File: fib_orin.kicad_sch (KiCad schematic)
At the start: 8 parts, among them J1201 Orin Nano

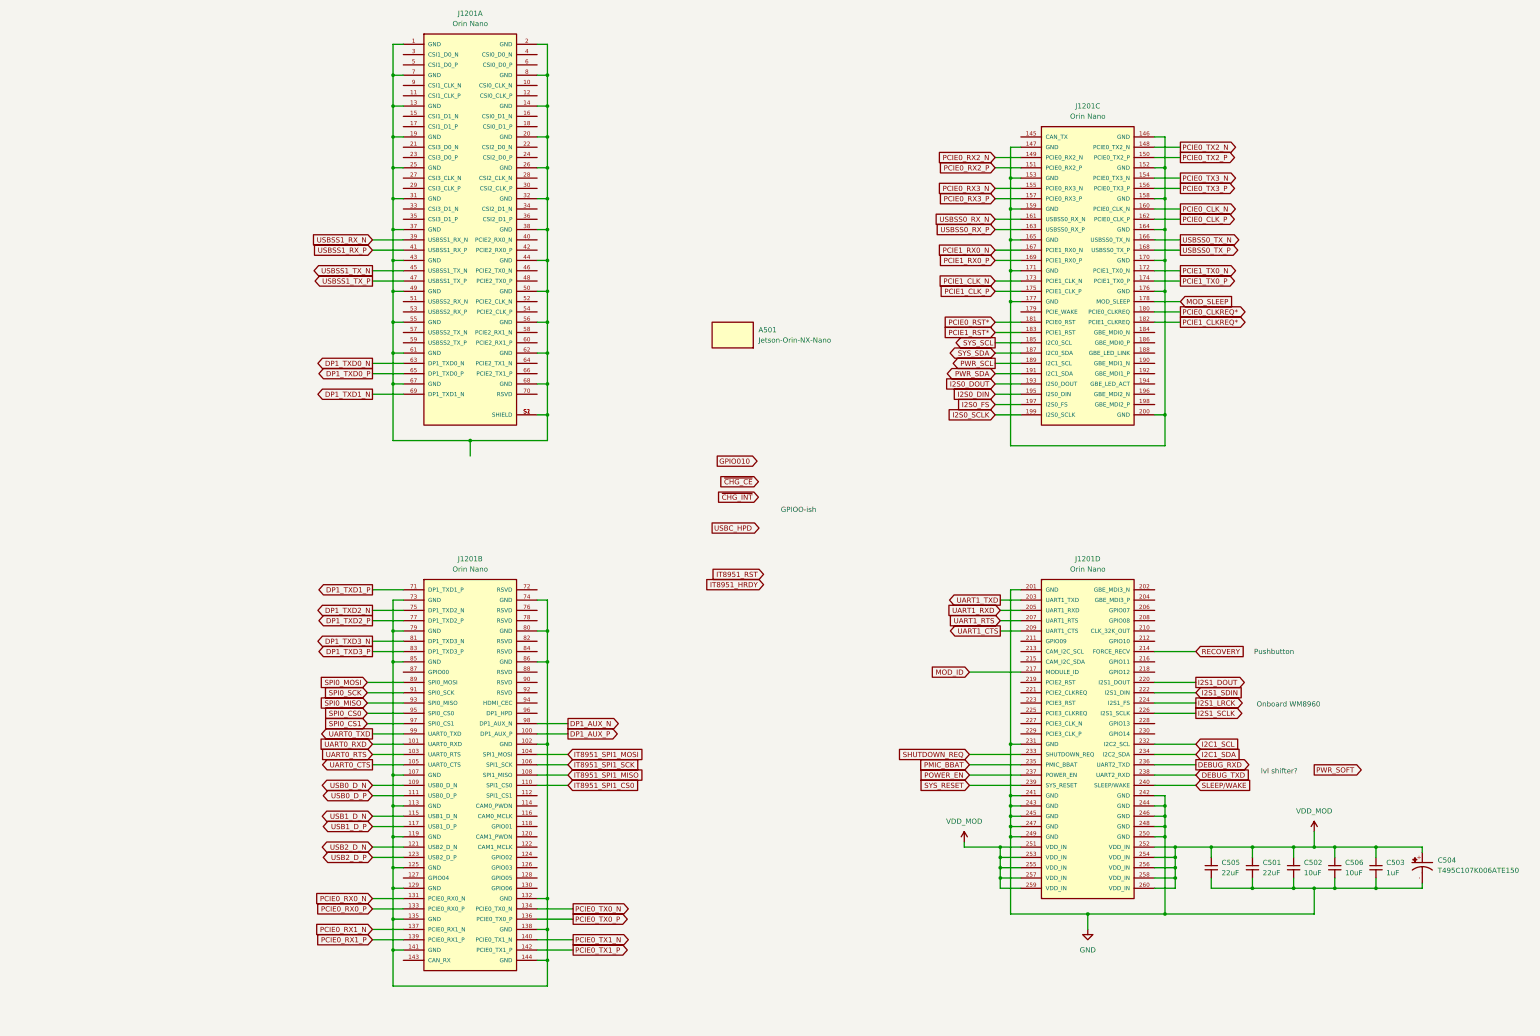
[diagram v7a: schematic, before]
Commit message: started routing the SODIMM, updated connector footprint, started arranging component into sub-areas
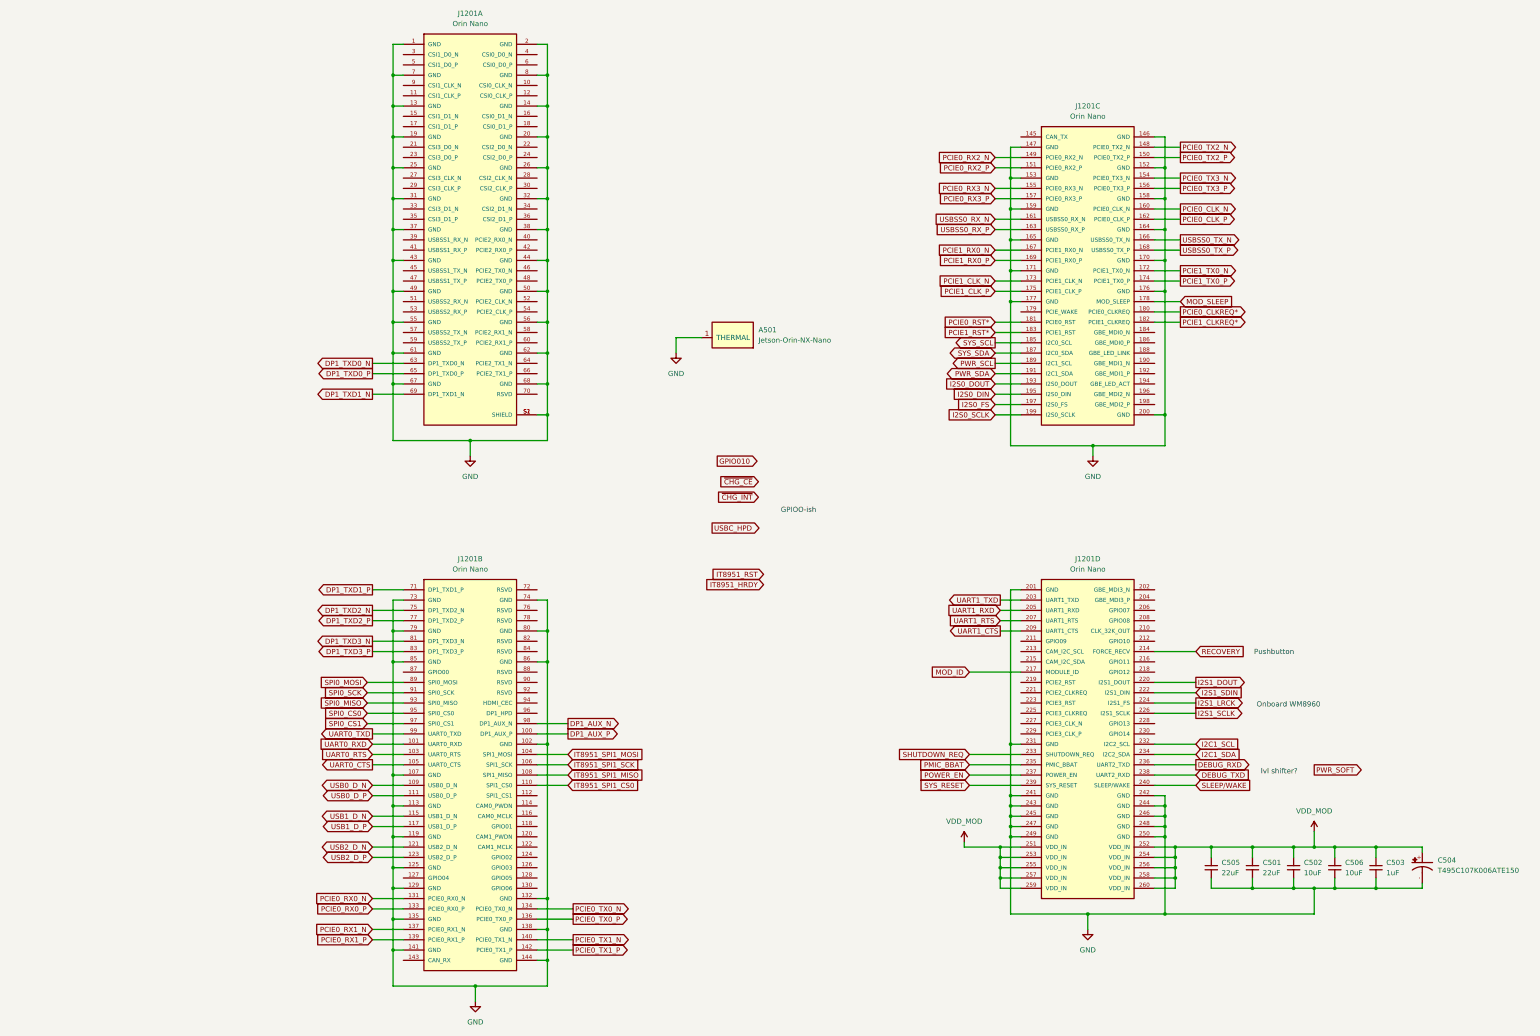
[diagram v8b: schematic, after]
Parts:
- J1201: footprint Fibel2:SODIMMx260 -> Fibel2:SODIMM_REVERSED
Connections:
- net GND: now also A501.1 (THERMAL), J1201.1 (GND), J1201.102 (GND), J1201.107 (GND), J1201.113 (GND), J1201.119 (GND), J1201.125 (GND), J1201.129 (GND), J1201.13 (GND), J1201.132 (GND), J1201.135 (GND), J1201.138 (GND), J1201.14 (GND), J1201.141 (GND), J1201.144 (GND), J1201.146 (GND), J1201.147 (GND), J1201.152 (GND), J1201.153 (GND), J1201.158 (GND), J1201.159 (GND), J1201.164 (GND), J1201.165 (GND), J1201.170 (GND), J1201.171 (GND), J1201.176 (GND), J1201.177 (GND), J1201.19 (GND), J1201.2 (GND), J1201.20 (GND), J1201.200 (GND), J1201.25 (GND), J1201.26 (GND), J1201.31 (GND), J1201.32 (GND), J1201.37 (GND), J1201.38 (GND), J1201.43 (GND), J1201.44 (GND), J1201.49 (GND), J1201.50 (GND), J1201.55 (GND), J1201.56 (GND), J1201.61 (GND), J1201.62 (GND), J1201.67 (GND), J1201.68 (GND), J1201.7 (GND), J1201.73 (GND), J1201.74 (GND), J1201.79 (GND), J1201.8 (GND), J1201.80 (GND), J1201.85 (GND), J1201.86 (GND), J1201.S1 (SHIELD), J1201.S2 (SHIELD)
- net USBSS1_RX_N: no longer names the net of J1201.39 (USBSS1_RX_N)
- net USBSS1_RX_P: no longer names the net of J1201.41 (USBSS1_RX_P)
- net USBSS1_TX_N: no longer names the net of J1201.45 (USBSS1_TX_N)
- net USBSS1_TX_P: no longer names the net of J1201.47 (USBSS1_TX_P)
